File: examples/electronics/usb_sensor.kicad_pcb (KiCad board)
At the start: 40 x 30 mm, 17 parts, among them J1 USB-Micro-B, J2 SWD, SW1 SPST, U1 AP2112K-3.3, U2 STM32F042, U3 SHT40

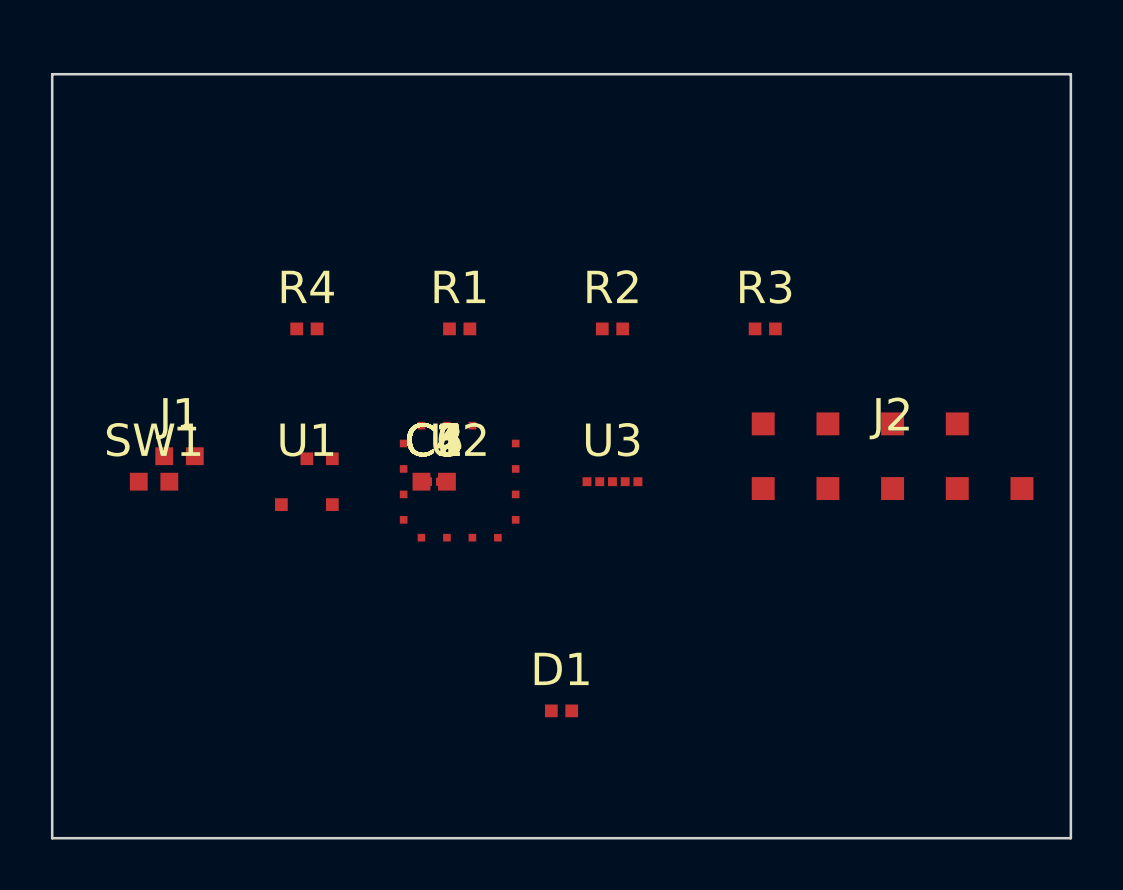
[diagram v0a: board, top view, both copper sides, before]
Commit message: feat(electronics): fab — collision-aware auto-placement (zero warnings)
The auto-placer now places every unplaced part on the first grid cell
whose footprint box fits the board AND clears every already-placed part
(MIN_CLEARANCE), and moves decouplers to ring points only when those
also clear. The pitch is a candidate lattice (3mm) since the collision
check does the real spacing. Result: the fixture board emits with ZERO
clearance warnings — the auto-placer never manufactures a warning it
could have avoided. Unknown footprints place best-effort (the layout
check reports them as errors). 2543 tests green; Praetor clean.
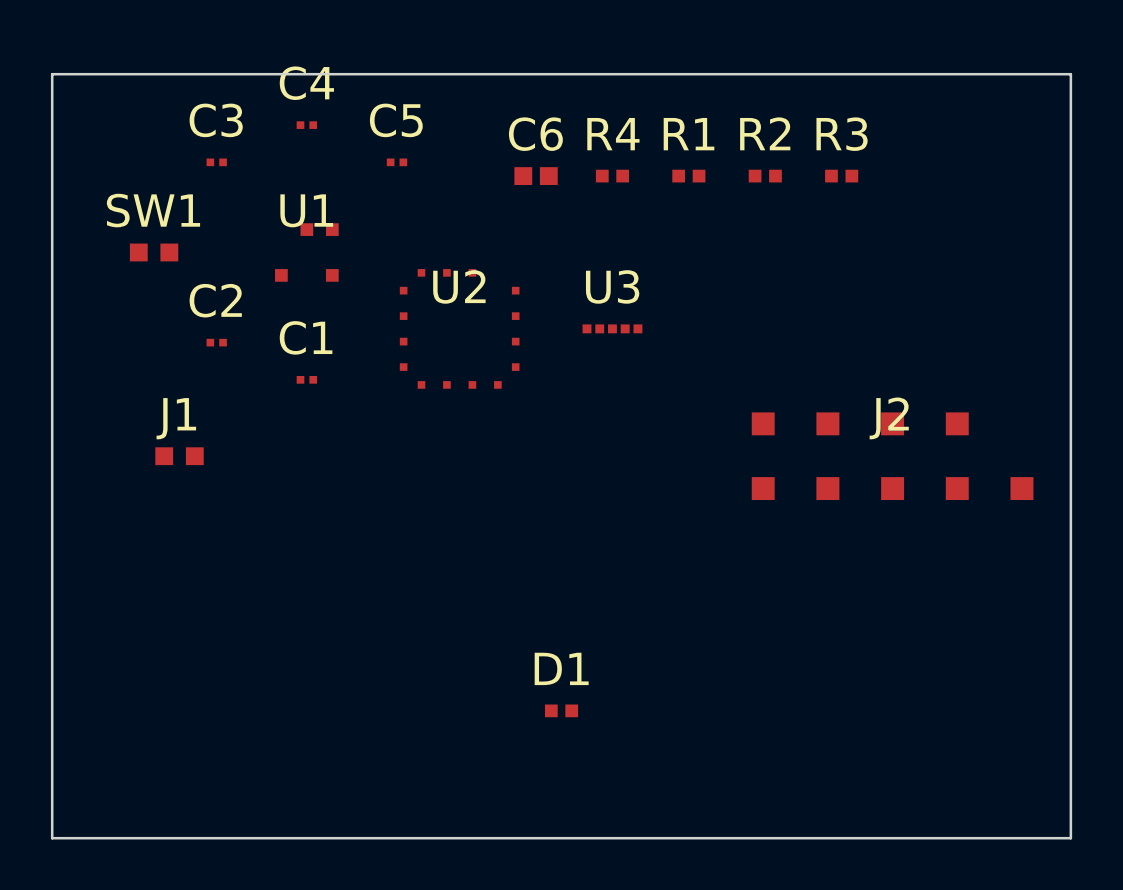
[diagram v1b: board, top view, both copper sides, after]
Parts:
- moved C3 15.2 mm to (6.46, 3.46)
- moved C4 14.9 mm to (10.0, 2.00)
- moved R4 13.4 mm to (22.0, 4.00)
- moved C6 12.6 mm to (19.0, 4.00)
- moved C5 12.6 mm to (13.5, 3.46)
- moved R1 10.8 mm to (25.0, 4.00)
- moved C2 10.1 mm to (6.46, 10.5)
- moved SW1 9.00 mm to (4.00, 7.00)
- moved U1 9.00 mm to (10.0, 7.00)
- moved R2 8.49 mm to (28.0, 4.00)
- moved R3 6.71 mm to (31.0, 4.00)
- moved C1 6.40 mm to (10.0, 12.0)
- moved U2 6.00 mm to (16.0, 10.0)
- moved U3 6.00 mm to (22.0, 10.0)
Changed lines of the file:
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@@
   (footprint "0402"
     (layer "F.Cu")
-    (at 15.00 16.00 0)
+    (at 10.00 12.00 0)
     (fp_text reference "C1" (at 0 -1.60) (layer "F.SilkS"))
     (fp_text value "100n" (at 0 1.60) (layer "F.Fab"))
@@
   (footprint "0402"
     (layer "F.Cu")
-    (at 15.00 16.00 0)
+    (at 6.46 10.54 0)
     (fp_text reference "C2" (at 0 -1.60) (layer "F.SilkS"))
     (fp_text value "100n" (at 0 1.60) (layer "F.Fab"))
@@
   (footprint "0402"
     (layer "F.Cu")
-    (at 15.00 16.00 0)
+    (at 6.46 3.46 0)
     (fp_text reference "C3" (at 0 -1.60) (layer "F.SilkS"))
     (fp_text value "100n" (at 0 1.60) (layer "F.Fab"))
@@
   (footprint "0402"
     (layer "F.Cu")
-    (at 15.00 16.00 0)
+    (at 10.00 2.00 0)
     (fp_text reference "C4" (at 0 -1.60) (layer "F.SilkS"))
     (fp_text value "100n" (at 0 1.60) (layer "F.Fab"))
@@
   (footprint "0402"
     (layer "F.Cu")
-    (at 15.00 16.00 0)
+    (at 13.54 3.46 0)
     (fp_text reference "C5" (at 0 -1.60) (layer "F.SilkS"))
     (fp_text value "100n" (at 0 1.60) (layer "F.Fab"))
@@
   (footprint "0805"
     (layer "F.Cu")
-    (at 15.00 16.00 0)
+    (at 19.00 4.00 0)
     (fp_text reference "C6" (at 0 -1.60) (layer "F.SilkS"))
     (fp_text value "10u" (at 0 1.60) (layer "F.Fab"))
@@
   (footprint "0603"
     (layer "F.Cu")
-    (at 10.00 10.00 0)
+    (at 22.00 4.00 0)
     (fp_text reference "R4" (at 0 -1.60) (layer "F.SilkS"))
     (fp_text value "10k" (at 0 1.60) (layer "F.Fab"))
@@
   (footprint "0603"
     (layer "F.Cu")
-    (at 16.00 10.00 0)
+    (at 25.00 4.00 0)
     (fp_text reference "R1" (at 0 -1.60) (layer "F.SilkS"))
     (fp_text value "TBD" (at 0 1.60) (layer "F.Fab"))
@@
   (footprint "0603"
     (layer "F.Cu")
-    (at 22.00 10.00 0)
+    (at 28.00 4.00 0)
     (fp_text reference "R2" (at 0 -1.60) (layer "F.SilkS"))
     (fp_text value "4k7" (at 0 1.60) (layer "F.Fab"))
@@
   (footprint "0603"
     (layer "F.Cu")
-    (at 28.00 10.00 0)
+    (at 31.00 4.00 0)
     (fp_text reference "R3" (at 0 -1.60) (layer "F.SilkS"))
     (fp_text value "4k7" (at 0 1.60) (layer "F.Fab"))
@@
   (footprint "SMD"
     (layer "F.Cu")
-    (at 4.00 16.00 0)
+    (at 4.00 7.00 0)
     (fp_text reference "SW1" (at 0 -1.60) (layer "F.SilkS"))
     (fp_text value "SPST" (at 0 1.60) (layer "F.Fab"))
@@
   (footprint "SOT-25"
     (layer "F.Cu")
-    (at 10.00 16.00 0)
+    (at 10.00 7.00 0)
     (fp_text reference "U1" (at 0 -1.60) (layer "F.SilkS"))
     (fp_text value "AP2112K-3.3" (at 0 1.60) (layer "F.Fab"))
@@
   (footprint "QFN-32"
     (layer "F.Cu")
-    (at 16.00 16.00 0)
+    (at 16.00 10.00 0)
     (fp_text reference "U2" (at 0 -1.60) (layer "F.SilkS"))
     (fp_text value "STM32F042" (at 0 1.60) (layer "F.Fab"))
@@
   (footprint "DFN-4"
     (layer "F.Cu")
-    (at 22.00 16.00 0)
+    (at 22.00 10.00 0)
     (fp_text reference "U3" (at 0 -1.60) (layer "F.SilkS"))
     (fp_text value "SHT40" (at 0 1.60) (layer "F.Fab"))

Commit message: feat(electronics): fab — auto-routing (compiler machinery, v1)
The compiler now routes the copper: each net's pads connect in a sorted
chain with Manhattan (L-shaped) tracks on F.Cu; a straight path that
crosses a part footprint is joggled over it (surfaced as a note); an
unresolvable crossing is accepted with a warning, never a silent short.
Deterministic — the routed board is byte-identical across runs. No
routing control surface: placement is the author's, the copper is the
compiler's. v1 is point-to-point; track DRC, vias, and multi-layer
planning are recorded follow-on.

6 jog notes on the fixture board (honest v1). routing.rs Praetor clean;
2543 lib tests green (board determinism now covers the segments).
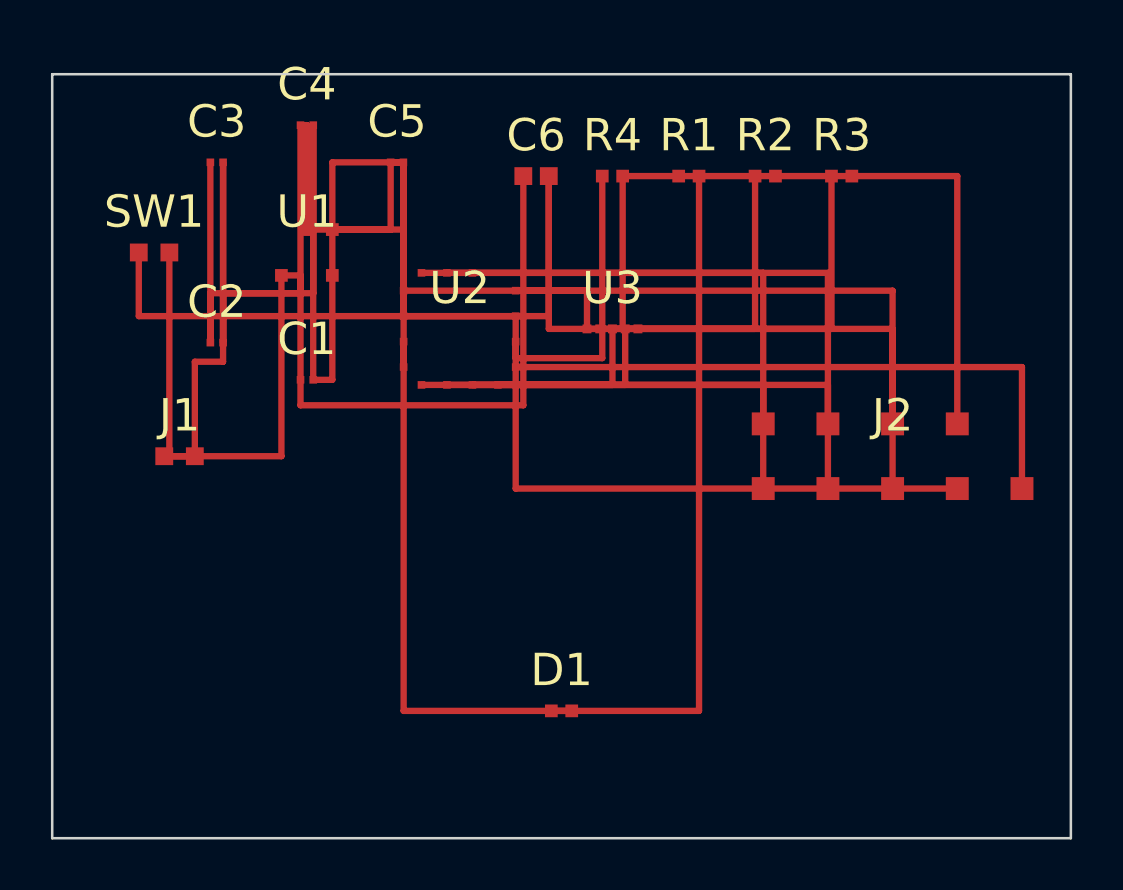
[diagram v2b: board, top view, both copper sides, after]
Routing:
- net GND: track 0.00 -> 103.4 mm
- net V3.3: track 0.00 -> 74.0 mm
- net V5: track 0.00 -> 35.3 mm
- net N6: track 0.00 -> 29.5 mm
- net N2: track 0.00 -> 26.8 mm
- net N12: track 0.00 -> 24.6 mm
- net N15: track 0.00 -> 23.4 mm
- net N11: track 0.00 -> 23.1 mm
- net N10: track 0.00 -> 22.6 mm
- net N4: track 0.00 -> 22.3 mm
- net N16: track 0.00 -> 21.9 mm
- net N8: track 0.00 -> 21.1 mm
- net N3: track 0.00 -> 18.3 mm
- net N14: track 0.00 -> 16.5 mm
- net N13: track 0.00 -> 15.0 mm
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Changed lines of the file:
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@@
     (pad "5" smd rect (at 1.00 0.00) (size 0.35 0.35) (layers "F.Cu" "F.Paste" "F.Mask") (net 1 "N1"))
   )
+  (segment (start 4.60 7.00) (end 4.60 15.00) (width 0.25) (layer "F.Cu") (net 1 "GND"))
+  (segment (start 4.60 15.00) (end 5.60 15.00) (width 0.25) (layer "F.Cu") (net 1 "GND"))
+  (segment (start 5.60 15.00) (end 5.60 11.29) (width 0.25) (layer "F.Cu") (net 1 "GND"))
+  (segment (start 5.60 11.29) (end 6.71 11.29) (width 0.25) (layer "F.Cu") (net 1 "GND"))
+  (segment (start 6.71 11.29) (end 6.71 3.46) (width 0.25) (layer "F.Cu") (net 1 "GND"))
+  (segment (start 6.71 3.46) (end 6.71 3.46) (width 0.25) (layer "F.Cu") (net 1 "GND"))
+  (segment (start 6.71 3.46) (end 6.71 10.54) (width 0.25) (layer "F.Cu") (net 1 "GND"))
+  (segment (start 6.71 10.54) (end 6.71 8.60) (width 0.25) (layer "F.Cu") (net 1 "GND"))
+  (segment (start 6.71 8.60) (end 10.25 8.60) (width 0.25) (layer "F.Cu") (net 1 "GND"))
+  (segment (start 10.25 8.60) (end 10.25 2.00) (width 0.25) (layer "F.Cu") (net 1 "GND"))
+  (segment (start 10.25 2.00) (end 10.25 8.60) (width 0.25) (layer "F.Cu") (net 1 "GND"))
+  (segment (start 10.25 8.60) (end 10.25 8.60) (width 0.25) (layer "F.Cu") (net 1 "GND"))
+  (segment (start 10.25 8.60) (end 10.25 12.00) (width 0.25) (layer "F.Cu") (net 1 "GND"))
+  (segment (start 10.25 12.00) (end 11.00 12.00) (width 0.25) (layer "F.Cu") (net 1 "GND"))
+  (segment (start 11.00 12.00) (end 11.00 7.90) (width 0.25) (layer "F.Cu") (net 1 "GND"))
+  (segment (start 11.00 7.90) (end 11.00 3.46) (width 0.25) (layer "F.Cu") (net 1 "GND"))
+  (segment (start 11.00 3.46) (end 13.79 3.46) (width 0.25) (layer "F.Cu") (net 1 "GND"))
+  (segment (start 13.79 3.46) (end 13.80 3.46) (width 0.25) (layer "F.Cu") (net 1 "GND"))
+  (segment (start 13.80 3.46) (end 13.80 9.50) (width 0.25) (layer "F.Cu") (net 1 "GND"))
+  (segment (start 13.80 9.50) (end 19.50 9.50) (width 0.25) (layer "F.Cu") (net 1 "GND"))
+  (segment (start 19.50 9.50) (end 19.50 4.00) (width 0.25) (layer "F.Cu") (net 1 "GND"))
+  (segment (start 19.50 4.00) (end 19.50 10.00) (width 0.25) (layer "F.Cu") (net 1 "GND"))
+  (segment (start 19.50 10.00) (end 21.50 10.00) (width 0.25) (layer "F.Cu") (net 1 "GND"))
+  (segment (start 21.50 10.00) (end 23.00 10.00) (width 0.25) (layer "F.Cu") (net 1 "GND"))
+  (segment (start 23.00 10.00) (end 23.00 10.00) (width 0.25) (layer "F.Cu") (net 1 "GND"))
+  (segment (start 23.00 10.00) (end 33.00 10.00) (width 0.25) (layer "F.Cu") (net 1 "GND"))
+  (segment (start 33.00 10.00) (end 33.00 13.73) (width 0.25) (layer "F.Cu") (net 1 "GND"))
+  (segment (start 19.60 25.00) (end 25.40 25.00) (width 0.25) (layer "F.Cu") (net 2 "N2"))
+  (segment (start 25.40 25.00) (end 25.40 4.00) (width 0.25) (layer "F.Cu") (net 2 "N2"))
+  (segment (start 17.50 12.20) (end 22.50 12.20) (width 0.25) (layer "F.Cu") (net 3 "N3"))
+  (segment (start 22.50 12.20) (end 22.50 10.00) (width 0.25) (layer "F.Cu") (net 3 "N3"))
+  (segment (start 22.50 10.00) (end 27.60 10.00) (width 0.25) (layer "F.Cu") (net 3 "N3"))
+  (segment (start 27.60 10.00) (end 27.60 4.00) (width 0.25) (layer "F.Cu") (net 3 "N3"))
+  (segment (start 16.50 12.20) (end 22.00 12.20) (width 0.25) (layer "F.Cu") (net 4 "N4"))
+  (segment (start 22.00 12.20) (end 22.00 10.00) (width 0.25) (layer "F.Cu") (net 4 "N4"))
+  (segment (start 22.00 10.00) (end 30.60 10.00) (width 0.25) (layer "F.Cu") (net 4 "N4"))
+  (segment (start 30.60 10.00) (end 30.60 4.00) (width 0.25) (layer "F.Cu") (net 4 "N4"))
+  (segment (start 6.21 3.46) (end 6.21 3.46) (width 0.25) (layer "F.Cu") (net 5 "V3.3"))
+  (segment (start 6.21 3.46) (end 6.21 10.54) (width 0.25) (layer "F.Cu") (net 5 "V3.3"))
+  (segment (start 6.21 10.54) (end 6.21 8.60) (width 0.25) (layer "F.Cu") (net 5 "V3.3"))
+  (segment (start 6.21 8.60) (end 9.75 8.60) (width 0.25) (layer "F.Cu") (net 5 "V3.3"))
+  (segment (start 9.75 8.60) (end 9.75 2.00) (width 0.25) (layer "F.Cu") (net 5 "V3.3"))
+  (segment (start 9.75 2.00) (end 10.00 2.00) (width 0.25) (layer "F.Cu") (net 5 "V3.3"))
+  (segment (start 10.00 2.00) (end 10.00 6.10) (width 0.25) (layer "F.Cu") (net 5 "V3.3"))
+  (segment (start 10.00 6.10) (end 13.29 6.10) (width 0.25) (layer "F.Cu") (net 5 "V3.3"))
+  (segment (start 13.29 6.10) (end 13.29 3.46) (width 0.25) (layer "F.Cu") (net 5 "V3.3"))
+  (segment (start 13.29 3.46) (end 13.80 3.46) (width 0.25) (layer "F.Cu") (net 5 "V3.3"))
+  (segment (start 13.80 3.46) (end 13.80 8.50) (width 0.25) (layer "F.Cu") (net 5 "V3.3"))
+  (segment (start 13.80 8.50) (end 21.00 8.50) (width 0.25) (layer "F.Cu") (net 5 "V3.3"))
+  (segment (start 21.00 8.50) (end 21.00 10.00) (width 0.25) (layer "F.Cu") (net 5 "V3.3"))
+  (segment (start 21.00 10.00) (end 22.40 10.00) (width 0.25) (layer "F.Cu") (net 5 "V3.3"))
+  (segment (start 22.40 10.00) (end 22.40 4.00) (width 0.25) (layer "F.Cu") (net 5 "V3.3"))
+  (segment (start 22.40 4.00) (end 24.60 4.00) (width 0.25) (layer "F.Cu") (net 5 "V3.3"))
+  (segment (start 24.60 4.00) (end 24.60 4.00) (width 0.25) (layer "F.Cu") (net 5 "V3.3"))
+  (segment (start 24.60 4.00) (end 28.40 4.00) (width 0.25) (layer "F.Cu") (net 5 "V3.3"))
+  (segment (start 28.40 4.00) (end 28.40 4.00) (width 0.25) (layer "F.Cu") (net 5 "V3.3"))
+  (segment (start 28.40 4.00) (end 31.40 4.00) (width 0.25) (layer "F.Cu") (net 5 "V3.3"))
+  (segment (start 31.40 4.00) (end 31.40 4.00) (width 0.25) (layer "F.Cu") (net 5 "V3.3"))
+  (segment (start 31.40 4.00) (end 35.54 4.00) (width 0.25) (layer "F.Cu") (net 5 "V3.3"))
+  (segment (start 35.54 4.00) (end 35.54 13.73) (width 0.25) (layer "F.Cu") (net 5 "V3.3"))
+  (segment (start 3.40 7.00) (end 3.40 9.50) (width 0.25) (layer "F.Cu") (net 6 "N6"))
+  (segment (start 3.40 9.50) (end 18.20 9.50) (width 0.25) (layer "F.Cu") (net 6 "N6"))
+  (segment (start 18.20 9.50) (end 18.20 11.15) (width 0.25) (layer "F.Cu") (net 6 "N6"))
+  (segment (start 18.20 11.15) (end 21.60 11.15) (width 0.25) (layer "F.Cu") (net 6 "N6"))
+  (segment (start 21.60 11.15) (end 21.60 4.00) (width 0.25) (layer "F.Cu") (net 6 "N6"))
+  (segment (start 4.40 15.00) (end 9.00 15.00) (width 0.25) (layer "F.Cu") (net 7 "V5"))
+  (segment (start 9.00 15.00) (end 9.00 7.90) (width 0.25) (layer "F.Cu") (net 7 "V5"))
+  (segment (start 9.00 7.90) (end 9.75 7.90) (width 0.25) (layer "F.Cu") (net 7 "V5"))
+  (segment (start 9.75 7.90) (end 9.75 12.00) (width 0.25) (layer "F.Cu") (net 7 "V5"))
+  (segment (start 9.75 12.00) (end 9.75 13.00) (width 0.25) (layer "F.Cu") (net 7 "V5"))
+  (segment (start 9.75 13.00) (end 18.50 13.00) (width 0.25) (layer "F.Cu") (net 7 "V5"))
+  (segment (start 18.50 13.00) (end 18.50 4.00) (width 0.25) (layer "F.Cu") (net 7 "V5"))
+  (segment (start 13.80 10.50) (end 13.80 25.00) (width 0.25) (layer "F.Cu") (net 8 "N8"))
+  (segment (start 13.80 25.00) (end 20.40 25.00) (width 0.25) (layer "F.Cu") (net 8 "N8"))
+  (segment (start 11.00 6.10) (end 13.80 6.10) (width 0.25) (layer "F.Cu") (net 9 "N9"))
+  (segment (start 13.80 6.10) (end 13.80 11.50) (width 0.25) (layer "F.Cu") (net 9 "N9"))
+  (segment (start 18.20 8.50) (end 33.00 8.50) (width 0.25) (layer "F.Cu") (net 10 "N10"))
+  (segment (start 33.00 8.50) (end 33.00 16.27) (width 0.25) (layer "F.Cu") (net 10 "N10"))
+  (segment (start 18.20 10.50) (end 18.20 16.27) (width 0.25) (layer "F.Cu") (net 11 "N11"))
+  (segment (start 18.20 16.27) (end 35.54 16.27) (width 0.25) (layer "F.Cu") (net 11 "N11"))
+  (segment (start 18.20 11.50) (end 38.08 11.50) (width 0.25) (layer "F.Cu") (net 12 "N12"))
+  (segment (start 38.08 11.50) (end 38.08 16.27) (width 0.25) (layer "F.Cu") (net 12 "N12"))
+  (segment (start 14.50 12.20) (end 27.92 12.20) (width 0.25) (layer "F.Cu") (net 13 "N13"))
+  (segment (start 27.92 12.20) (end 27.92 13.73) (width 0.25) (layer "F.Cu") (net 13 "N13"))
+  (segment (start 15.50 12.20) (end 30.46 12.20) (width 0.25) (layer "F.Cu") (net 14 "N14"))
+  (segment (start 30.46 12.20) (end 30.46 13.73) (width 0.25) (layer "F.Cu") (net 14 "N14"))
+  (segment (start 15.50 7.80) (end 30.46 7.80) (width 0.25) (layer "F.Cu") (net 15 "N15"))
+  (segment (start 30.46 7.80) (end 30.46 16.27) (width 0.25) (layer "F.Cu") (net 15 "N15"))
+  (segment (start 14.50 7.80) (end 27.92 7.80) (width 0.25) (layer "F.Cu") (net 16 "N16"))
+  (segment (start 27.92 7.80) (end 27.92 16.27) (width 0.25) (layer "F.Cu") (net 16 "N16"))
 )

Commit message: feat(electronics): component laws Slice 5 — stdlib laws and fixtures
Add generic dimensioned law parameters on pin-bearing component types
(spec ForwardVoltage: Volt; spec DynamicResistance: Ohm;), including
type-level quantity defaults. Unknown spec names remain rejected outside
component bodies.

- stdlib Resistor and Wire declare always-active laws
- stdlib Diode and Led declare forward/reverse piecewise laws
- later component declarations shadow prelude declarations, so local
  same-named types cannot inherit stdlib laws by accident
- migrate led_blinker to stdlib laws and structured datasheet physics;
  the solver proves its 4.4 mA operating point
- migrate usb_sensor resistance values to structured specs; keep its
  local Resistor law-free until SPST conditional-topology state exists
- document the law mechanism and remaining fixture migration boundary

Full lib suite green; Praetor no new diagnostics; both fixtures emit.
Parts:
- R1: value TBD -> 330R
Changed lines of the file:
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@@
     (at 25.00 4.00 0)
     (fp_text reference "R1" (at 0 -1.60) (layer "F.SilkS"))
-    (fp_text value "TBD" (at 0 1.60) (layer "F.Fab"))
+    (fp_text value "330R" (at 0 1.60) (layer "F.Fab"))
     (pad "1" smd rect (at -0.40 0.00) (size 0.50 0.50) (layers "F.Cu" "F.Paste" "F.Mask") (net 5 "N5"))
     (pad "2" smd rect (at 0.40 0.00) (size 0.50 0.50) (layers "F.Cu" "F.Paste" "F.Mask") (net 2 "N2"))
